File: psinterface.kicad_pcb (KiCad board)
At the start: 2 copper layers, 74.8 x 49.5 mm, 7 parts, among them J1 Conn_02x04_Top_Bottom, J2 Conn_01x10, J3 Conn_02x06_Top_Bottom, J4 Conn_01x05, J5 Conn_01x01, J6 Conn_01x03, SW1 SW_SPDT

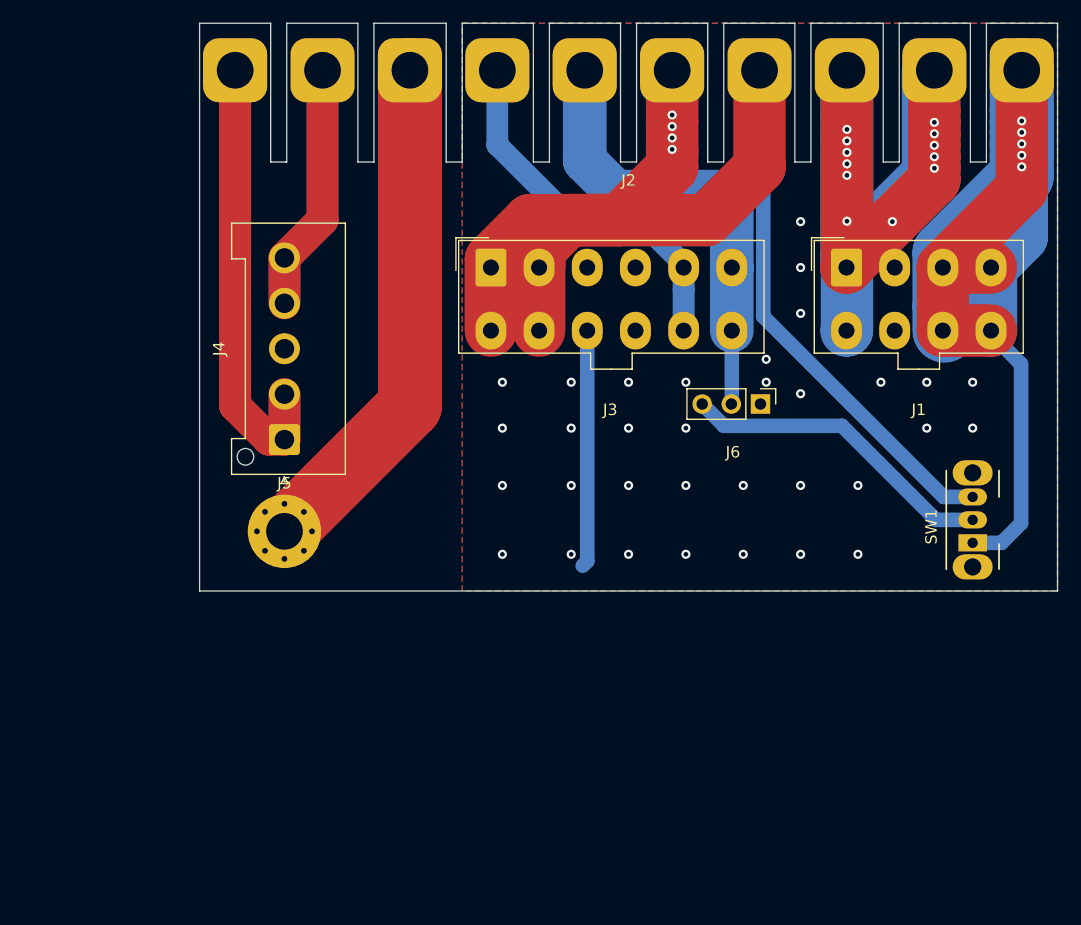
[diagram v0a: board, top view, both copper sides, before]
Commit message: Reduced sized, added text labels
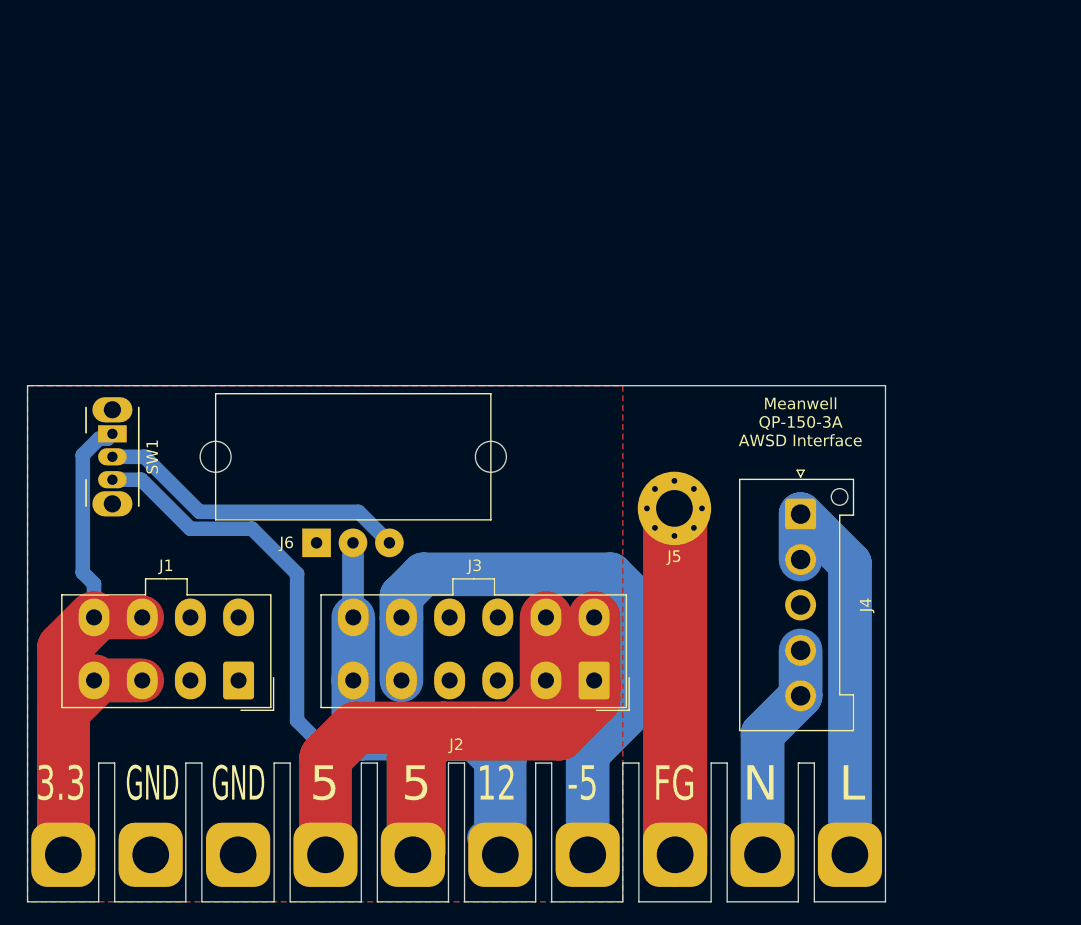
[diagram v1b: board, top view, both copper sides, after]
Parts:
- added LCD: MountingHole_2.7mm_M2.5, MountingHole:MountingHole_2.7mm_M2.5, F.Cu at (117.0, 100.5)
- added LCD: MountingHole_2.7mm_M2.5, MountingHole:MountingHole_2.7mm_M2.5, F.Cu at (141.0, 100.5)
- J6: footprint Connector_PinHeader_2.54mm:PinHeader_1x03_P2.54mm_Vertical -> Connector_Wire:SolderWirePad_1x03_P3.175mm_Drill1mm
- moved SW1 75.6 mm to (108.0, 98.5), turned to 270 degrees
- moved J2 70.0 mm to (138.0, 135.2), turned to 180 degrees
- moved J1 64.1 mm to (119.0, 120.0), turned to 180 degrees
- moved J4 45.5 mm to (168.0, 105.5), turned to 270 degrees
- moved J6 40.5 mm to (125.8, 108.0), turned to 0 degrees
- moved J3 37.1 mm to (150.0, 120.0), turned to 180 degrees
- moved J5 34.1 mm to (157.0, 105.0), turned to 180 degrees
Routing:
- net Net-(J1-Pad1): track 118.8 -> 0.00 mm, vias 45 -> 0
- net Net-(J1-Pad3): track 106.1 -> 64.4 mm, vias 5 -> 0
- net Net-(J2-Pad7): track 32.9 -> 53.3 mm
- net Net-(J2-Pad4): track 125.4 -> 142.9 mm, vias 4 -> 0
- net Net-(J2-Pad8): track 44.7 -> 30.2 mm
- net Net-(J2-Pad10): track 38.7 -> 35.4 mm
- net Net-(J2-Pad9): track 21.7 -> 19.2 mm
- net Net-(J2-Pad6): track 39.7 -> 40.6 mm
- net Net-(J6-Pad3): track 27.8 -> 27.3 mm
- removed copper zone on B.Cu, net Net-(J1-Pad1)
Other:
- board size 74.8 x 49.5 mm -> 74.8 x 45 mm
- board text added: "-5"
- board text added: "12"
- board text added: "3.3"
- board text added: "5"
- board text added: "FG"
- board text added: "GND"
- board text added: "L"
- board text added: "Meanwell QP-150-3A AWSD Interface"
- board text added: "N"

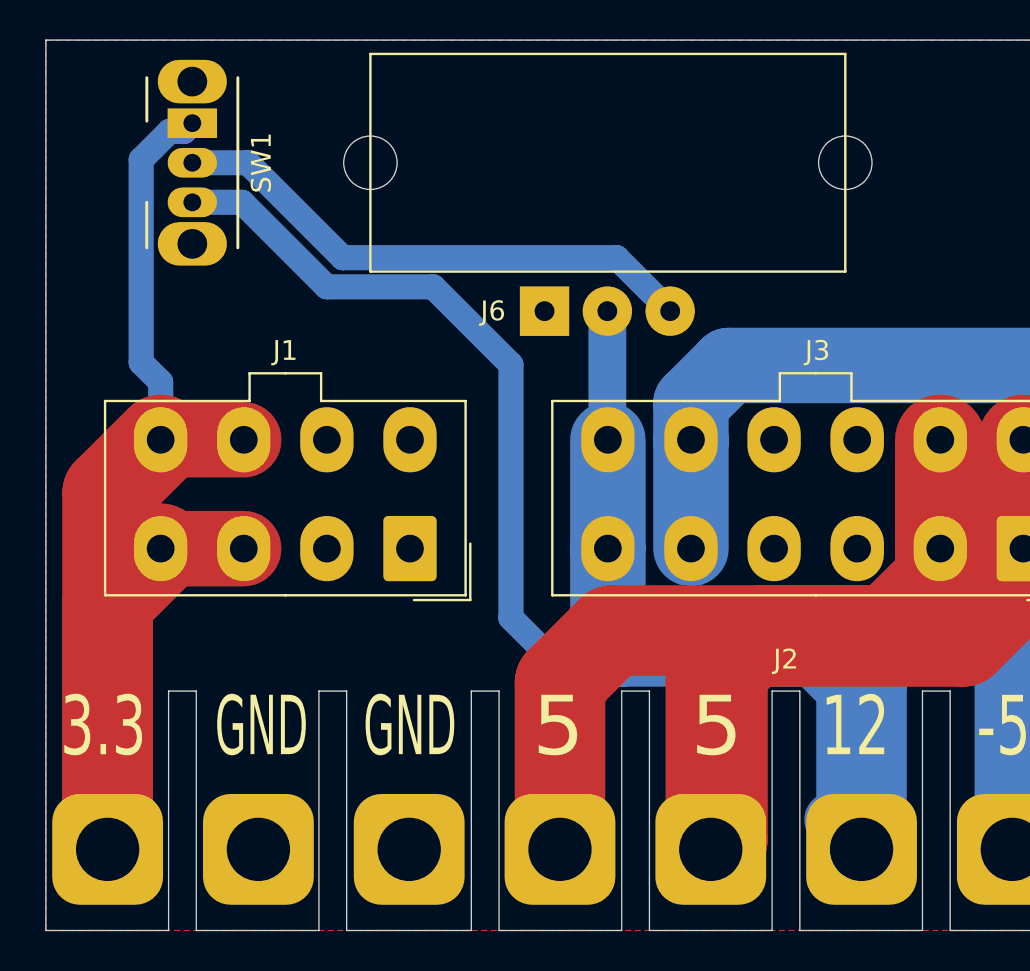
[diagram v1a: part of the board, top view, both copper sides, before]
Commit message: Changed LCD mounting holes to 28mm
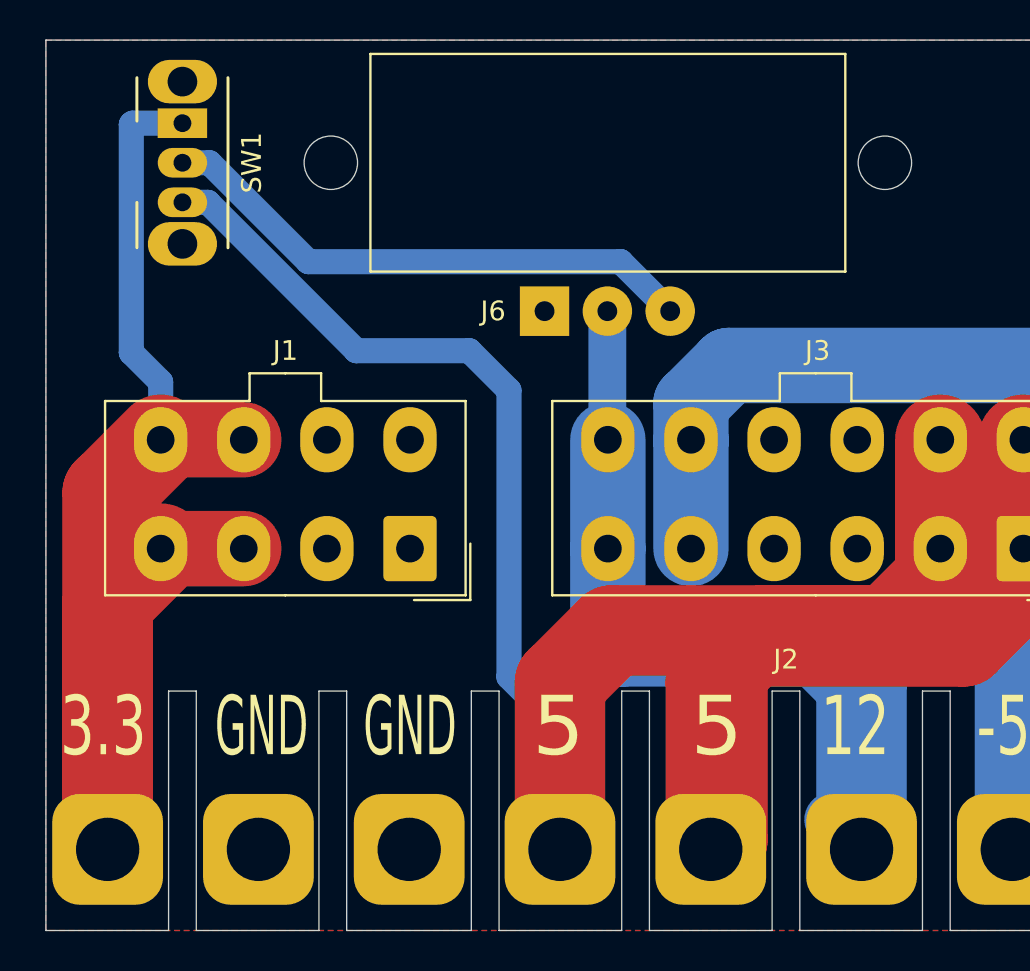
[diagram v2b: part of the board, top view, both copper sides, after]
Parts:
- moved LCD 2.00 mm to (115.0, 100.5)
- moved LCD 2.00 mm to (143.0, 100.5)
- moved SW1 0.50 mm to (107.5, 98.5)
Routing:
- net Net-(J1-Pad3): track 64.4 -> 65.7 mm
- net Net-(J6-Pad3): track 27.3 -> 27.8 mm
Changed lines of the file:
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@@
   )
   (setup
-    (last_trace_width 0.25)
+    (last_trace_width 1.27)
     (user_trace_width 0.254)
     (user_trace_width 1.27)
@@
   )
   (module MountingHole:MountingHole_2.7mm_M2.5 (layer F.Cu)
-    (at 117 100.5)
+    (at 115 100.5)
     (descr "Mounting Hole 2.7mm, no annular, M2.5")
     (tags "mounting hole 2.7mm no annular m2.5")
@@
   )
   (module MountingHole:MountingHole_2.7mm_M2.5 (layer F.Cu)
-    (at 141 100.5)
+    (at 143 100.5)
     (descr "Mounting Hole 2.7mm, no annular, M2.5")
     (tags "mounting hole 2.7mm no annular m2.5")
@@
   )
   (module Button_Switch_THT:SW_CuK_OS102011MA1QN1_SPDT_Angled (layer F.Cu)
-    (at 108 98.5 270)
+    (at 107.5 98.5 270)
     (descr "CuK miniature slide switch, OS series, SPDT, right angle, http://www.ckswitches.com/media/1428/os.pdf")
     (tags "switch SPDT")
@@
   (segment (start 110.6 114.5) (end 106.4 114.5) (width 3.81) (layer F.Cu) (net 2) (status 30))
   (segment (start 110.6 120) (end 106.4 120) (width 3.81) (layer F.Cu) (net 2) (status 30))
-  (segment (start 106.4 111.58) (end 106.4 114.5) (width 1.27) (layer B.Cu) (net 2) (status 20))
-  (segment (start 105.41499 110.59499) (end 106.4 111.58) (width 1.27) (layer B.Cu) (net 2))
-  (segment (start 106.843468 98.91499) (end 105.41499 100.343468) (width 1.27) (layer B.Cu) (net 2) (status 10))
-  (segment (start 105.41499 100.343468) (end 105.41499 110.59499) (width 1.27) (layer B.Cu) (net 2))
-  (segment (start 107.58501 98.91499) (end 106.843468 98.91499) (width 1.27) (layer B.Cu) (net 2) (status 30))
-  (segment (start 108 98.5) (end 107.58501 98.91499) (width 1.27) (layer B.Cu) (net 2) (status 30))
   (segment (start 103.72 117.18) (end 103.72 135.2) (width 4.572) (layer F.Cu) (net 2))
   (segment (start 106.4 114.5) (end 103.72 117.18) (width 4.572) (layer F.Cu) (net 2))
   (segment (start 103.72 122.68) (end 103.72 135.2) (width 4.572) (layer F.Cu) (net 2))
   (segment (start 106.4 120) (end 103.72 122.68) (width 4.572) (layer F.Cu) (net 2))
+  (segment (start 104.98 98.5) (end 107.5 98.5) (width 1.27) (layer B.Cu) (net 2))
+  (segment (start 104.91499 98.56501) (end 104.98 98.5) (width 1.27) (layer B.Cu) (net 2))
+  (segment (start 104.91499 110.09499) (end 104.91499 98.56501) (width 1.27) (layer B.Cu) (net 2))
+  (segment (start 106.4 111.58) (end 104.91499 110.09499) (width 1.27) (layer B.Cu) (net 2))
+  (segment (start 106.4 114.5) (end 106.4 111.58) (width 1.27) (layer B.Cu) (net 2))
   (segment (start 145.8 120.722) (end 145.8 114.5) (width 4.572) (layer F.Cu) (net 3) (status 30))
   (segment (start 145.8 121.524937) (end 145.8 120.722) (width 4.572) (layer F.Cu) (net 3) (status 30))
@@
   (segment (start 134.3 135.2) (end 134.78899 134.71101) (width 4.572) (layer F.Cu) (net 3) (status 30))
   (segment (start 134.2 135.2) (end 134.3 135.2) (width 4.572) (layer F.Cu) (net 3) (status 30))
-  (segment (start 114.79001 106.77001) (end 110.52 102.5) (width 1.27) (layer B.Cu) (net 3))
-  (segment (start 126.58 125.98) (end 124.1 123.5) (width 1.27) (layer B.Cu) (net 3))
-  (segment (start 110.52 102.5) (end 108 102.5) (width 1.27) (layer B.Cu) (net 3))
-  (segment (start 124.1 123.5) (end 124.1 110.7) (width 1.27) (layer B.Cu) (net 3))
-  (segment (start 126.58 135.2) (end 126.58 125.98) (width 1.27) (layer B.Cu) (net 3))
-  (segment (start 124.1 110.7) (end 120.17001 106.77001) (width 1.27) (layer B.Cu) (net 3))
-  (segment (start 120.17001 106.77001) (end 114.79001 106.77001) (width 1.27) (layer B.Cu) (net 3))
   (segment (start 134.2 126.748896) (end 134.2 135.2) (width 4.572) (layer F.Cu) (net 3))
   (segment (start 136.259906 124.68899) (end 134.2 126.748896) (width 4.572) (layer F.Cu) (net 3))
@@
   (segment (start 150 121.65) (end 146.96101 124.68899) (width 4.572) (layer F.Cu) (net 3))
   (segment (start 150 120) (end 150 121.65) (width 4.572) (layer F.Cu) (net 3))
+  (segment (start 108.786517 102.5) (end 116.286517 110) (width 1.27) (layer B.Cu) (net 3))
+  (segment (start 107.5 102.5) (end 108.786517 102.5) (width 1.27) (layer B.Cu) (net 3))
+  (segment (start 116.286517 110) (end 122 110) (width 1.27) (layer B.Cu) (net 3))
+  (segment (start 122 110) (end 124 112) (width 1.27) (layer B.Cu) (net 3))
+  (segment (start 126.58 132.4) (end 126.58 135.2) (width 1.27) (layer B.Cu) (net 3))
+  (segment (start 126.58 129.063763) (end 126.58 132.4) (width 1.27) (layer B.Cu) (net 3))
+  (segment (start 124 126.483763) (end 126.58 129.063763) (width 1.27) (layer B.Cu) (net 3))
+  (segment (start 124 112) (end 124 126.483763) (width 1.27) (layer B.Cu) (net 3))
   (segment (start 140.32201 133.70201) (end 141.82 135.2) (width 2.794) (layer B.Cu) (net 4) (status 30))
   (segment (start 129.04 114.46) (end 129 114.5) (width 1.27) (layer B.Cu) (net 4) (status 30))
@@
   (segment (start 164.68 135.2) (end 164.68 124.66) (width 3.81) (layer B.Cu) (net 8) (status 10))
   (segment (start 168 117.38) (end 168 121.34) (width 3.81) (layer B.Cu) (net 8) (status 30))
-  (segment (start 108 100.5) (end 110.8 100.5) (width 1.27) (layer B.Cu) (net 9))
-  (segment (start 110.8 100.5) (end 115.6 105.3) (width 1.27) (layer B.Cu) (net 9))
-  (segment (start 129.45 105.3) (end 132.15 108) (width 1.27) (layer B.Cu) (net 9))
-  (segment (start 115.6 105.3) (end 129.45 105.3) (width 1.27) (layer B.Cu) (net 9))
+  (segment (start 107.5 100.5) (end 108.865425 100.5) (width 1.27) (layer B.Cu) (net 9))
+  (segment (start 108.865425 100.5) (end 113.865425 105.5) (width 1.27) (layer B.Cu) (net 9))
+  (segment (start 129.65 105.5) (end 132.15 108) (width 1.27) (layer B.Cu) (net 9))
+  (segment (start 113.865425 105.5) (end 129.65 105.5) (width 1.27) (layer B.Cu) (net 9))
   (zone (net 1) (net_name "Net-(J1-Pad1)") (layer F.Cu) (hatch edge 0.508)
     (connect_pads yes (clearance 0.508))

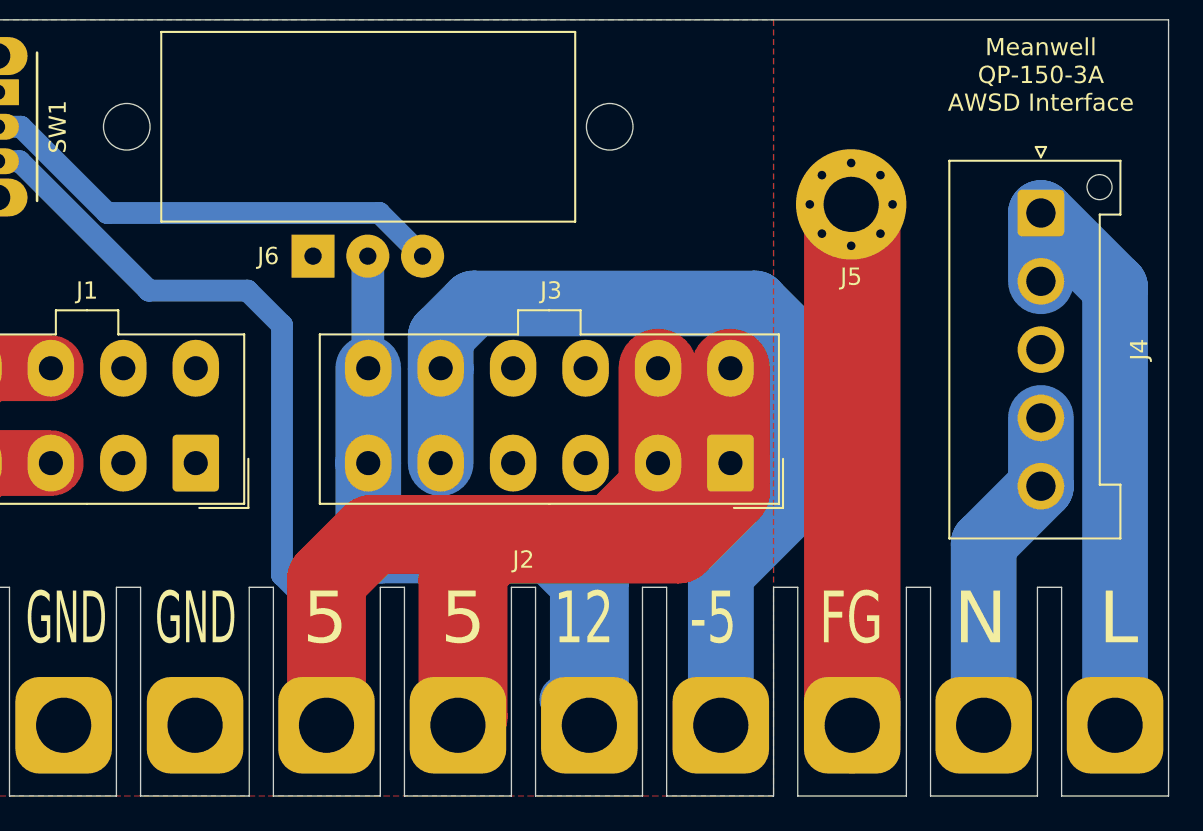
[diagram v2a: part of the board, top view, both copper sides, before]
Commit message: Corrected AC wiring, updated parts list
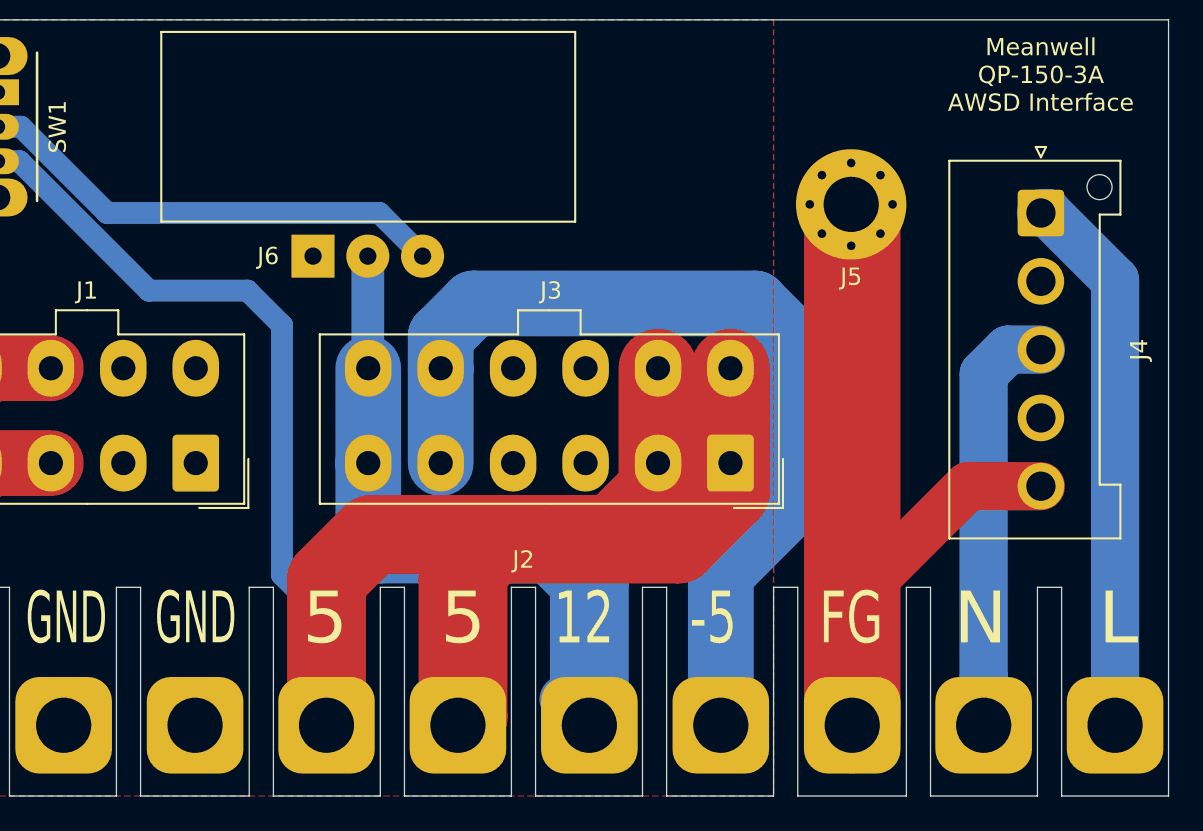
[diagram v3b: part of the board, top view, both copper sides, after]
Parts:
- removed LCD (x2): MountingHole_2.7mm_M2.5, MountingHole:MountingHole_2.7mm_M2.5
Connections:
- J4 pad 2: Net-(J2-Pad10) -> (no net)
- J4 pad 3: (no net) -> Net-(J2-Pad9)
- J4 pad 4: Net-(J2-Pad9) -> (no net)
- J4 pad 5: Net-(J2-Pad9) -> Net-(J2-Pad8)
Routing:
- net Net-(J2-Pad8): track 30.2 -> 51.1 mm
- net Net-(J2-Pad9): track 19.2 -> 24.3 mm
- net Net-(J2-Pad10): track 35.4 -> 31.7 mm
